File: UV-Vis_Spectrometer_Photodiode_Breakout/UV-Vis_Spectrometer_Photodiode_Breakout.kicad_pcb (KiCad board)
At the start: 2 copper layers, 48 parts, among them J1 Conn_01x05, J2 Conn_01x02, J3 Conn_01x02, Q1 BSS138BK,215, Q2 BSS138BK,215, Q3 BSS138BK,215, U1 TLV8811DBVR, U2 LM317BS-TR, U3 LTC2451

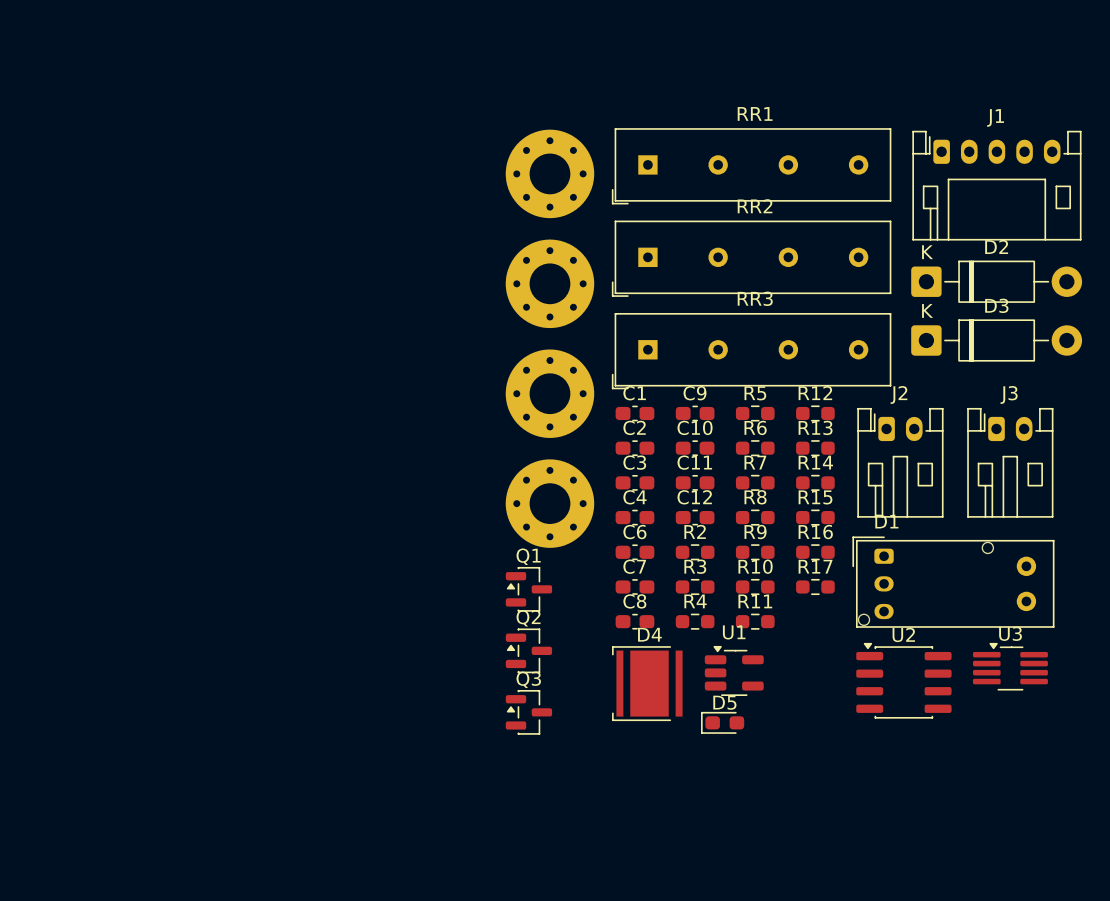
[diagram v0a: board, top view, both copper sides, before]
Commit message: Made footprint for photodiode. Made basic layout for PCB.
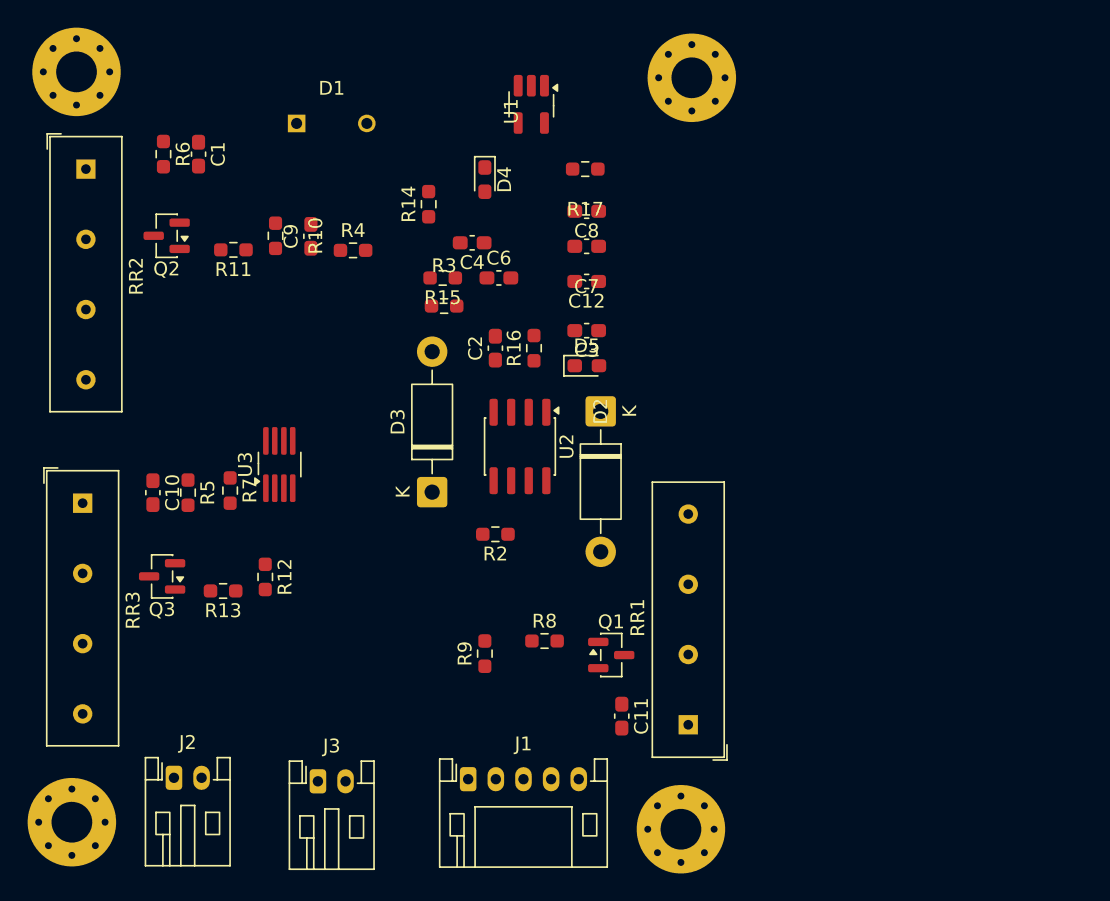
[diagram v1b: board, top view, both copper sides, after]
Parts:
- D1: footprint OptoDevice:Kodenshi_LG206D -> PhotoDiode_BPW21R:BPW21R
- D4: footprint LED_SMD:LED_Cree-XHP50_3V_HighDensity -> LED_SMD:LED_0603_1608Metric_Pad1.05x0.95mm_HandSolder
- D5: footprint Diode_SMD:D_0603_1608Metric_Pad1.05x0.95mm_HandSolder -> LED_SMD:LED_0603_1608Metric_Pad1.05x0.95mm_HandSolder
- moved J2 57.4 mm to (95.8, 99.7)
- moved J1 56.9 mm to (117.1, 99.8)
- moved J3 55.3 mm to (106.2, 99.9)
- moved U3 54.9 mm to (103.4, 77.0), turned to 90 degrees
- moved D1 50.8 mm to (107.2, 52.3)
- moved R6 47.8 mm to (95.0, 54.5), turned to -90 degrees
- moved U6 46.4 mm to (88.4, 102.9)
- moved R11 46.4 mm to (100.1, 61.5), turned to 180 degrees
- moved R13 44.1 mm to (99.3, 86.1), turned to 180 degrees
- moved U1 43.7 mm to (121.6, 50.9), turned to -90 degrees
- moved R10 43.0 mm to (103.1, 60.5), turned to -90 degrees
- moved RR3 42.4 mm to (89.2, 79.8), turned to -90 degrees
- moved R12 41.5 mm to (102.4, 85.1), turned to -90 degrees
- moved R5 41.4 mm to (96.8, 79.0), turned to -90 degrees
- moved RR2 41.2 mm to (89.4, 55.6), turned to -90 degrees
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
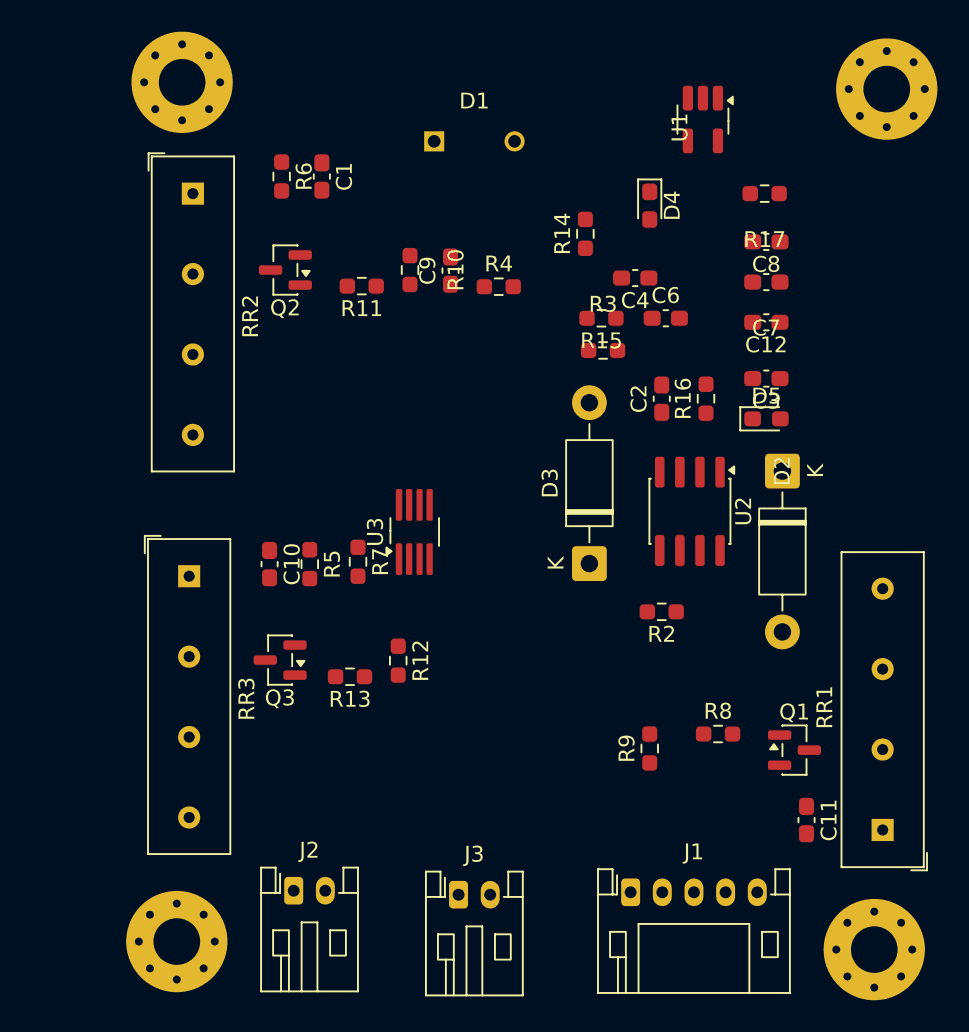
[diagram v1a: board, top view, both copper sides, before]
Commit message: Attempted to make layout smaller.
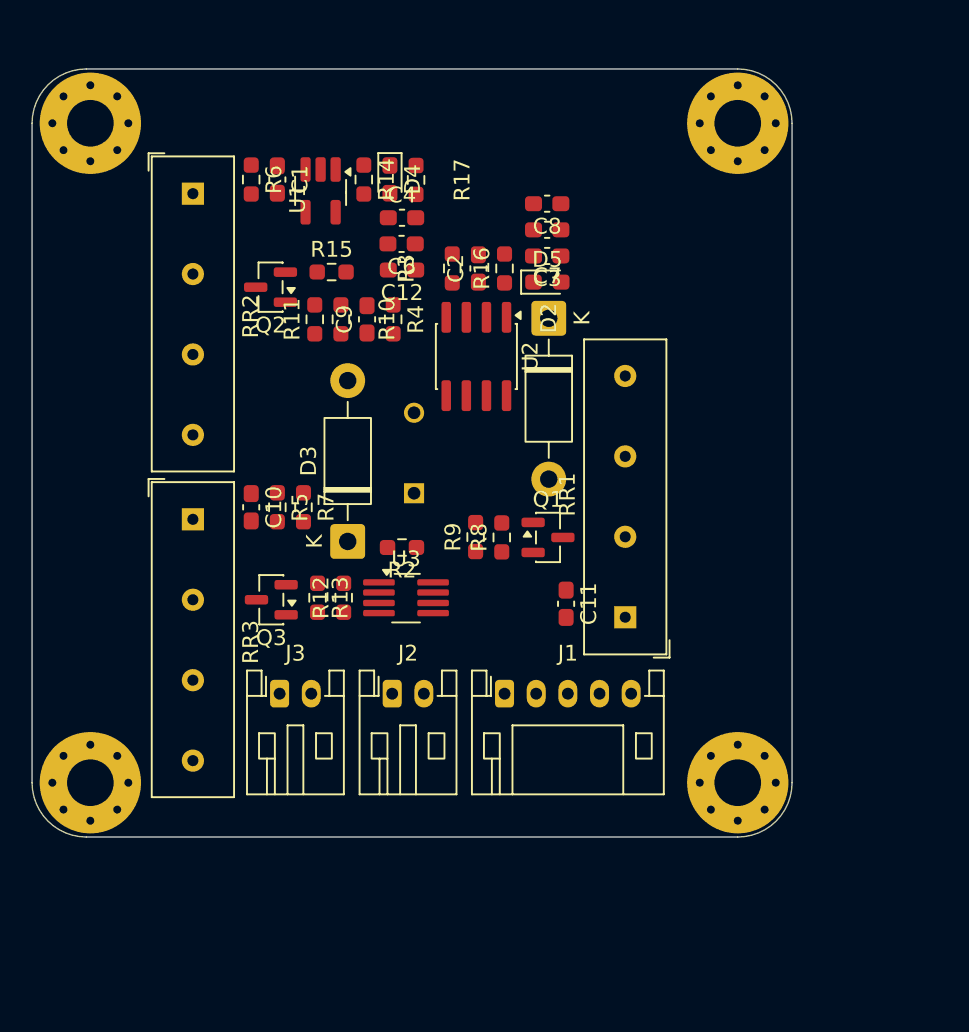
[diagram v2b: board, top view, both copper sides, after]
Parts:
- D1: moved to B.Cu
- moved U1 24.6 mm to (97.5, 55.5)
- moved C12 23.2 mm to (102.6, 60.5)
- moved R17 22.0 mm to (103.5, 54.8), turned to -90 degrees
- moved RR1 21.1 mm to (116.7, 82.4)
- moved Q1 20.6 mm to (111.8, 77.3)
- moved C11 20.4 mm to (113.0, 81.5)
- moved D1 20.1 mm to (103.4, 72.0), turned to 90 degrees
- moved R8 18.5 mm to (108.9, 77.3), turned to 90 degrees
- moved D2 17.6 mm to (111.9, 63.5)
- moved C6 17.3 mm to (102.6, 58.8), turned to 180 degrees
- moved R9 17.3 mm to (107.3, 77.3)
- moved R15 17.3 mm to (98.2, 60.6), turned to 0 degrees
- moved J3 17.0 mm to (94.9, 87.2)
- moved R2 16.9 mm to (102.6, 78.0)
- moved U2 16.7 mm to (107.3, 65.9)
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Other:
- board outline added: 48 x 48.5 mm

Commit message: Moved the layout around a bit.
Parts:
- D2, D3: value 1N4001 -> CDSU101A; footprint Diode_THT:D_DO-41_SOD81_P10.16mm_Horizontal -> Diode_SMD:D_0603_1608Metric_Pad1.05x0.95mm_HandSolder
- moved C4 130.4 mm to (213.9, 125.2)
- moved U2 124.1 mm to (213.6, 129.9)
- moved R3 123.4 mm to (211.3, 124.3)
- moved D3 123.1 mm to (209.8, 131.7)
- moved C3 120.7 mm to (214.8, 122.6), turned to -90 degrees
- moved C2 120.6 mm to (209.7, 124.3)
- moved R2 118.4 mm to (208.2, 131.7), turned to 90 degrees
- moved D2 117.2 mm to (213.1, 122.6)
- moved R14 95.2 mm to (191.4, 27.5)
- moved R15 93.1 mm to (186.2, 30.1)
- moved C12 90.4 mm to (185.3, 24.0), turned to -90 degrees
- moved RR1 78.3 mm to (49.7, 41.9), turned to 0 degrees
- moved C11 76.1 mm to (50.5, 38.1), turned to 180 degrees
- moved R11 74.9 mm to (172.0, 67.3), turned to 180 degrees
- moved Q2 73.7 mm to (167.8, 66.6)
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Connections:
- net Net-(D1-K) renamed /IN-

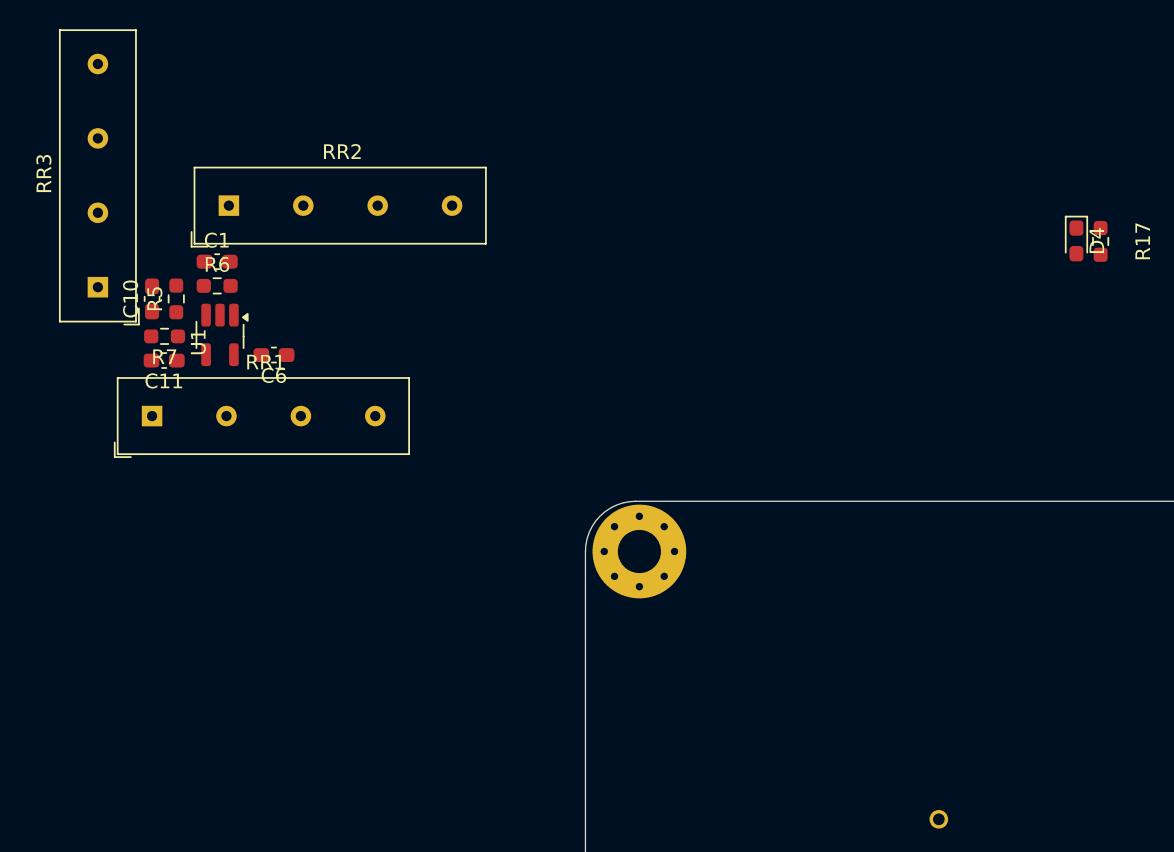
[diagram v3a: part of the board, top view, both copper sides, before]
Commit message: Updated footprint for Reed Relays.
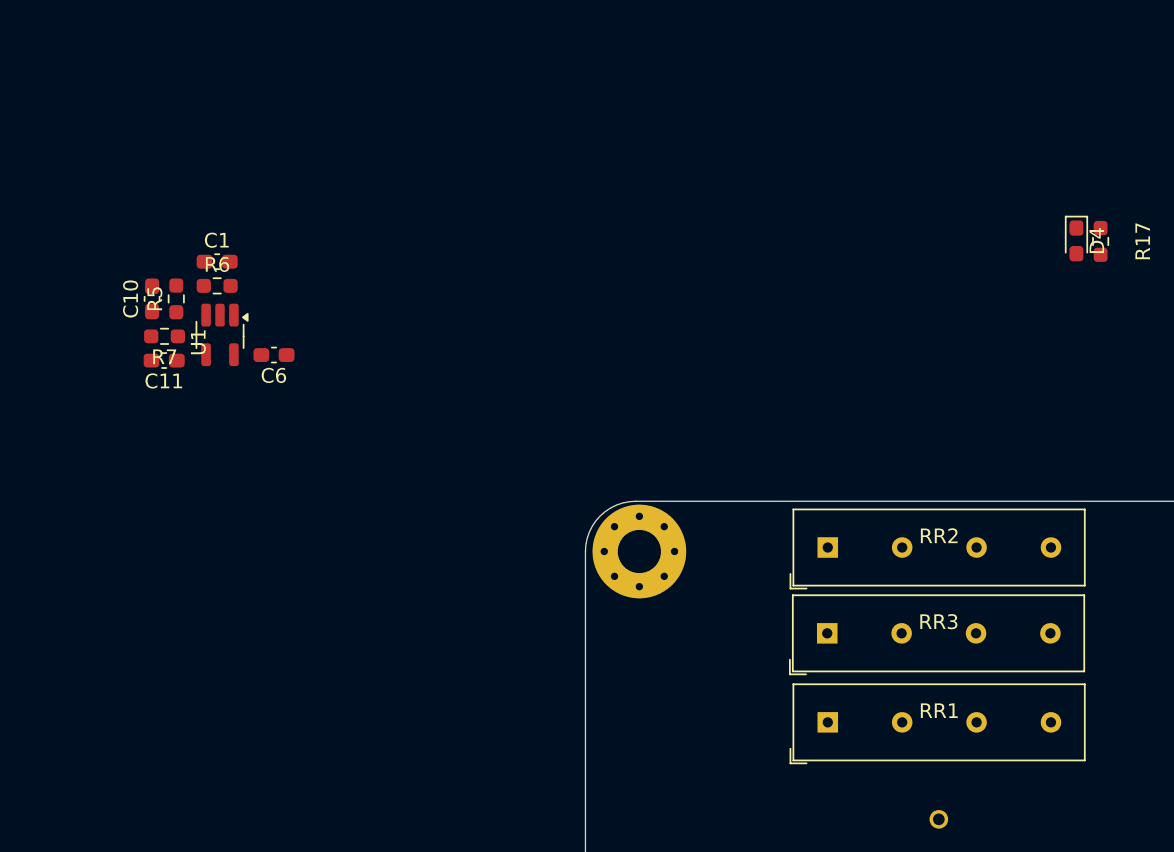
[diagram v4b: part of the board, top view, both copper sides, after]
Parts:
- RR1, RR2, RR3: footprint Relay_THT:Relay_SPST_StandexMeder_SIL_Form1A -> UV_Vis_Library:Relay_SPDT_9007_05_00
- moved RR3 62.0 mm to (103.4, 56.5), turned to 0 degrees
- moved RR1 57.6 mm to (103.4, 62.6)
- moved RR2 53.7 mm to (103.4, 50.6)

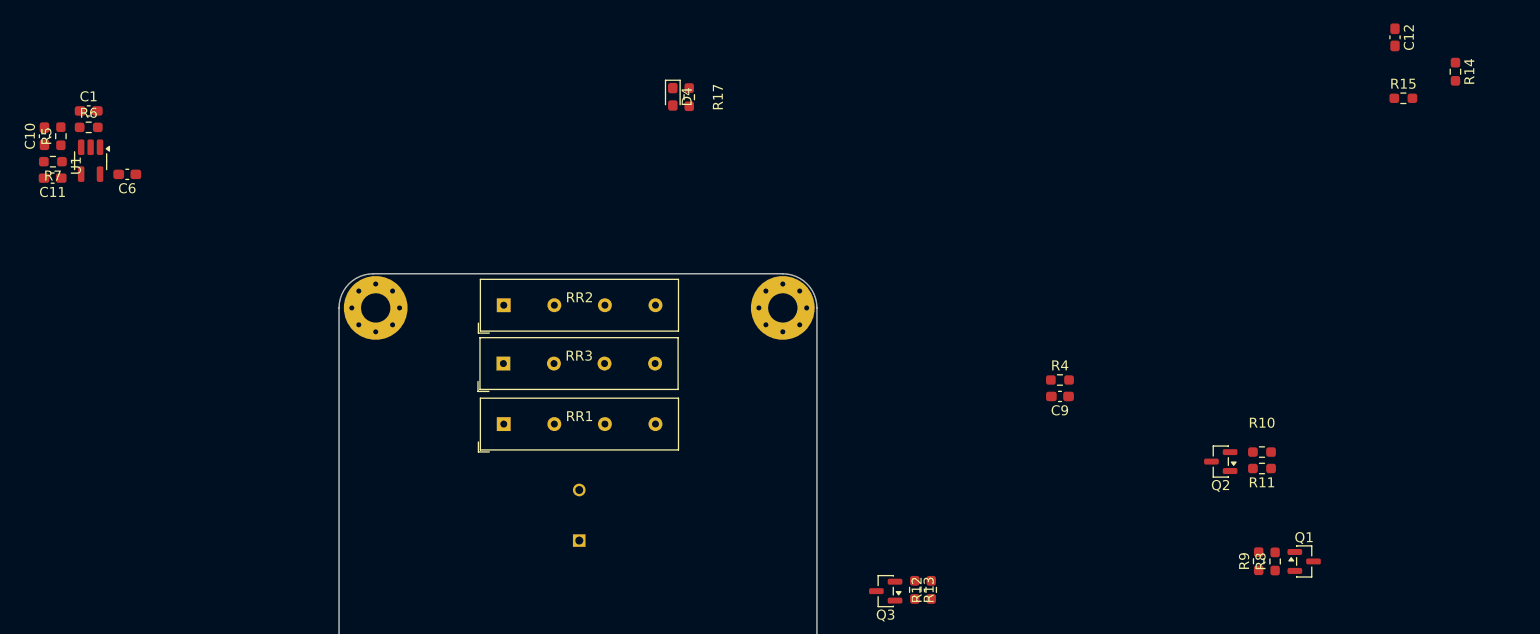
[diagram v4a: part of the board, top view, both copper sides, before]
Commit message: Added guard trace.
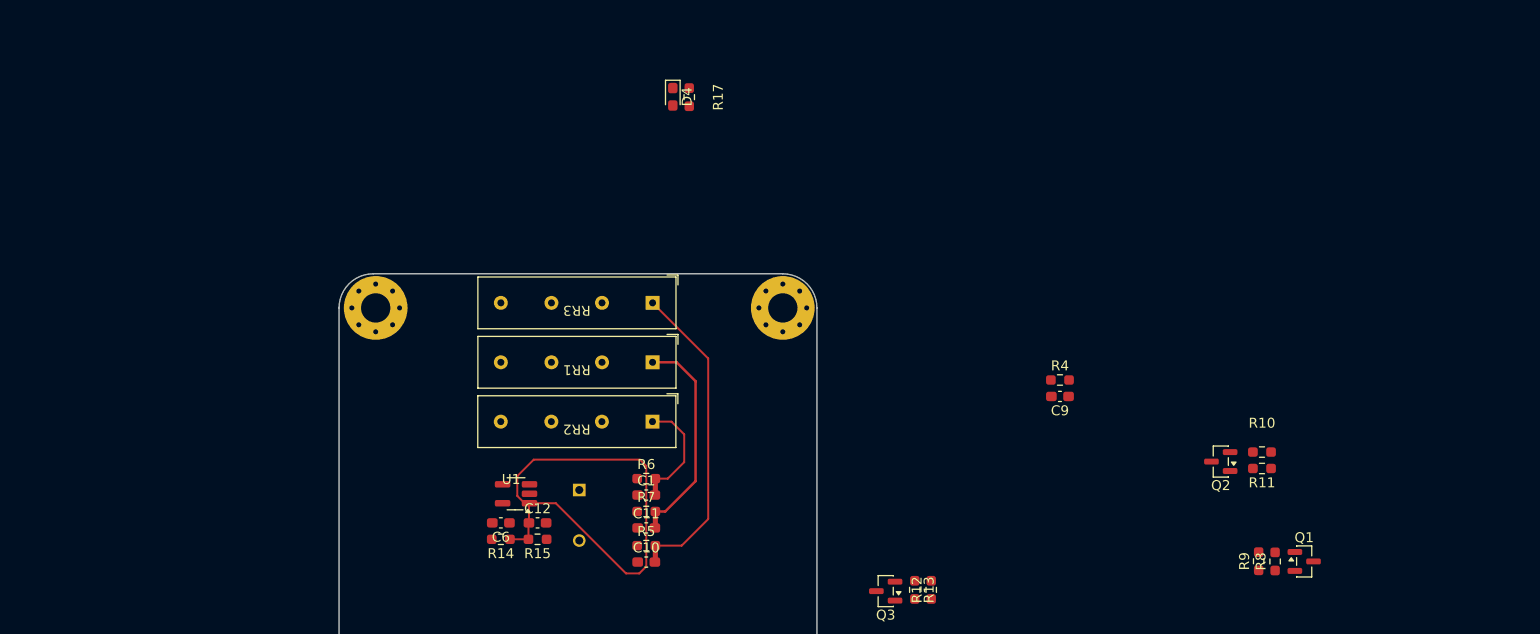
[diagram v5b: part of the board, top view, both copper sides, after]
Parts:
- moved R14 106.8 mm to (95.5, 74.4), turned to 180 degrees
- moved C12 99.0 mm to (99.2, 72.8), turned to 0 degrees
- moved R15 97.6 mm to (99.2, 74.4), turned to 180 degrees
- moved C10 74.1 mm to (110.1, 76.7), turned to 0 degrees
- moved R5 71.8 mm to (110.1, 75.1), turned to 0 degrees
- moved C11 69.2 mm to (110.1, 73.3), turned to 0 degrees
- moved R7 69.2 mm to (110.1, 71.6), turned to 0 degrees
- moved C1 68.0 mm to (110.1, 70.0)
- moved R6 66.2 mm to (110.1, 68.3)
- moved U1 54.3 mm to (97.0, 69.8), turned to 180 degrees
- moved C6 51.3 mm to (95.5, 72.8)
- moved RR2 12.2 mm to (103.1, 62.9), turned to 180 degrees
- moved RR1 5.69 mm to (103.1, 56.9), turned to 180 degrees
- moved RR3 5.58 mm to (103.1, 50.9), turned to 180 degrees
- turned D1 to -90 degrees
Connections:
- net Net-(C1-Pad2) renamed /SW2
- net Net-(C10-Pad2) renamed /SW3
- net Net-(C11-Pad2) renamed /SW1
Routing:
- net V_{REF}: track 0.00 -> 48.0 mm
- net /SW3: track 0.00 -> 32.1 mm
- net /SW1: track 0.00 -> 22.1 mm
- net /SW2: track 0.00 -> 11.8 mm

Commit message: General layout of components clean. Board is dimensioned.
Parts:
- moved D3 126.2 mm to (95.4, 78.4), turned to 0 degrees
- moved U2 125.8 mm to (97.2, 82.2), turned to 180 degrees
- moved R2 125.4 mm to (95.4, 76.7), turned to 0 degrees
- moved C4 119.9 mm to (101.9, 82.5), turned to -90 degrees
- moved R3 117.3 mm to (102.8, 79.9), turned to 0 degrees
- moved C3 117.0 mm to (104.6, 83.3), turned to 180 degrees
- moved C2 116.4 mm to (102.8, 78.2), turned to 0 degrees
- moved D2 116.0 mm to (104.6, 81.7), turned to 180 degrees
- moved R8 84.0 mm to (92.3, 54.5), turned to 0 degrees
- moved Q1 82.7 mm to (96.2, 55.4)
- moved R9 81.9 mm to (92.3, 56.2), turned to 180 degrees
- moved R11 80.1 mm to (92.3, 58.4), turned to 0 degrees
- moved R10 79.8 mm to (92.3, 60.1), turned to 180 degrees
- moved R4 72.6 mm to (81.8, 78.2), turned to 180 degrees
- moved Q2 72.0 mm to (96.2, 59.2), turned to 0 degrees
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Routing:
- net /SW3: track 32.1 -> 1.67 mm
- net /SW1: track 22.1 -> 1.67 mm
- net /SW2: track 11.8 -> 1.67 mm
